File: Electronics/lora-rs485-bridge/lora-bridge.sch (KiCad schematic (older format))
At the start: 21 parts

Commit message: Some PCB routing is done
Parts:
- removed C?: C, symbol Device:C
- removed D4: NUP4004M5T1G, Housings_SOT-23_SOT-143_TSOT-6:SOT-23-5, symbol miceuz:TVS-ARRAY
- removed J?: USB_B_Micro, symbol Connector:USB_B_Micro
- added C10: 4.7u, Capacitor_SMD:C_0603_1608Metric, symbol Device:C
- added D1, D4: D_TVS_x2_AAC, miceuz-lib:SC89, symbol Device:D_TVS_x2_AAC
- added J9: USB micro, Connectors_USB:USB_Micro-B_Vertical_Molex-105133-0001, symbol Connector:USB_B_Micro
- C1, C2: renamed from C?; value C -> 22p; footprint (none) -> Capacitor_SMD:C_0603_1608Metric
- C3, C4, C5, C6, C8, C9: renamed from C?; value C -> 1u; footprint (none) -> Capacitor_SMD:C_0603_1608Metric
- J1: renamed from J?; footprint (none) -> TerminalBlock_RND:TerminalBlock_RND_205-00001_Pitch5.00mm
- J2: renamed from J?; footprint (none) -> Connector_Coaxial:SMA_Amphenol_901-144_Vertical; Manufacturer (none) -> TE Connectivity AMP Connectors; PartNo (none) -> 5-1814832-1
- J3, J4: renamed from J?; footprint (none) -> TerminalBlock_RND:TerminalBlock_RND_205-00003_Pitch5.00mm
- R1: renamed from R?; value R -> 10k; footprint (none) -> Resistor_SMD:R_0603_1608Metric
- SW1, SW2: renamed from SW?; footprint (none) -> Button_Switch_SMD:SW_Push_1P1T_NO_6x6mm_H9.5mm
- U2: renamed from U?; Manufacturer (none) -> Microchip; PartNo (none) -> ATSAMD21G18A-AUT
- U3: renamed from U?; Manufacturer (none) -> HopeRF; PartNo (none) -> RFM95W-868S2
- Y1: renamed from Y?; footprint (none) -> Crystals:Crystal_SMD_3215-2pin_3.2x1.5mm; Manufacturer (none) -> EPSON; PartNo (none) -> FC-135 32.7680KA-A5
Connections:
- net labels added: ANTENNA, DIO01, DIO02
- wire segments 55 -> 58

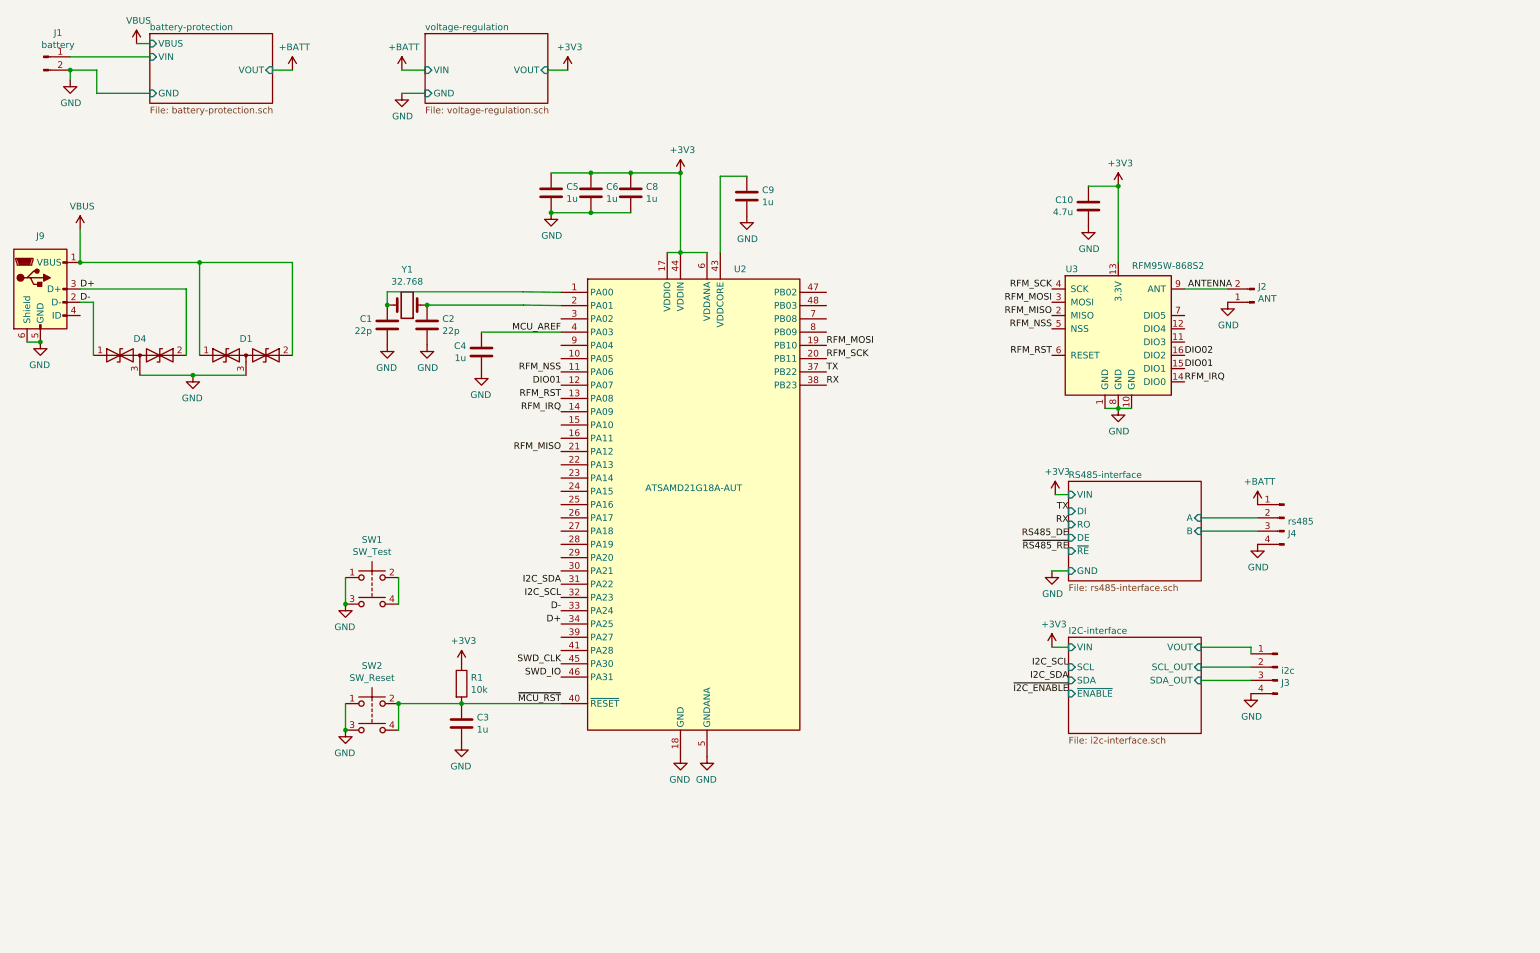
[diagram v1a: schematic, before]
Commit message: Add ESD protection to i2c lines, change VIN TVS diode to higher voltage, add series resistors to SPI lines, compress the PCB to be at width of typical 4xAA battery holder
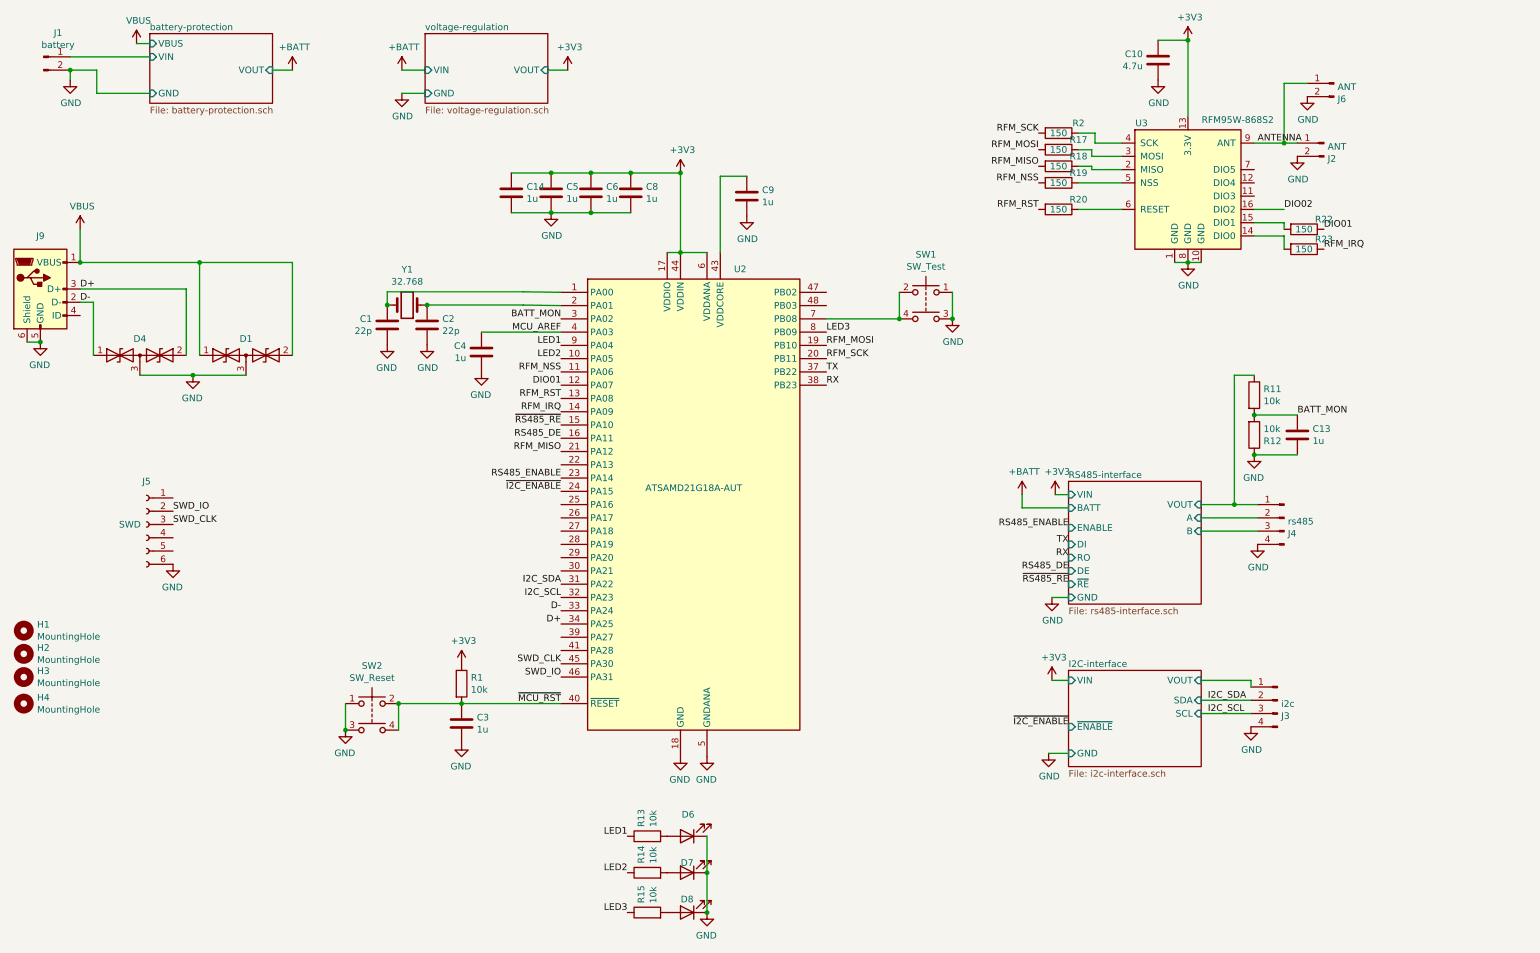
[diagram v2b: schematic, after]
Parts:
- added C13, C14: 1u, Capacitor_SMD:C_0603_1608Metric, symbol Device:C
- added D6, D7, D8: LED, LED_SMD:LED_0603_1608Metric, symbol Device:LED
- added H1, H2, H3, H4: MountingHole, Mounting_Holes:MountingHole_3.2mm_M3_DIN965, symbol Mechanical:MountingHole
- added J5: SWD, miceuz-lib:TC2030-MCP-NL, symbol Connector:Conn_01x06_Female
- added J6: ANT, miceuz-lib:U.FL_TEConnectivity_2334884_1, symbol Connector:Conn_01x02_Male
- added R11, R12, R13, R14, R15: 10k, Resistor_SMD:R_0603_1608Metric, symbol Device:R
- added R17, R18, R19, R2, R20, R22, R23: 150, Resistor_SMD:R_0603_1608Metric, symbol Device:R
- C10: Manufacturer SAMSUNG -> TDK; PartNo CL10A475KP8NNNC -> C1608X5R1C475K080AE
- J1: footprint TerminalBlock_RND:TerminalBlock_RND_205-00001_Pitch5.00mm -> TerminalBlock_MetzConnect:TerminalBlock_MetzConnect_Type101_RT01602HBWC_Pitch5.08mm
- J3, J4: footprint TerminalBlock_RND:TerminalBlock_RND_205-00003_Pitch5.00mm -> TerminalBlock_MetzConnect:TerminalBlock_MetzConnect_Type101_RT01604HBWC_Pitch5.08mm
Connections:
- net I2C-interface/SCL_OUT is gone; now on net I2C_SDA: J3.2 (Pin_2)
- net I2C-interface/SDA_OUT is gone; now on net I2C_SCL: J3.3 (Pin_3)
- net +3V3: now also C14.1
- net +BATT: no longer J4.1 (Pin_1)
- net ANTENNA: now also J2.1 (Pin_1), J6.1 (Pin_1); no longer J2.2 (Pin_2)
- net DIO01: now also R22.1; no longer U3.15 (DIO1)
- net GND: now also J2.2 (Pin_2), C13.2, C14.2, D6.1 (K), D7.1 (K), D8.1 (K), J5.6 (Pin_6), J6.2 (Pin_2), R12.1; no longer J2.1 (Pin_1)
- net RFM_IRQ: now also R23.1; no longer U3.14 (DIO0)
- net RFM_MISO: now also R18.2; no longer U3.2 (MISO)
- net RFM_MOSI: now also R17.2; no longer U3.3 (MOSI)
- net RFM_NSS: now also R19.2; no longer U3.5 (NSS)
- net RFM_RST: now also R20.2; no longer U3.6 (RESET)
- net RFM_SCK: now also R2.2; no longer U3.4 (SCK)
- net RS485_DE: now also U2.16 (PA11)
- net SWD_CLK: now also J5.3 (Pin_3)
- net SWD_IO: now also J5.2 (Pin_2)
- net ~I2C_ENABLE: now also U2.24 (PA15)
- net ~RS485_RE: now also U2.15 (PA10)
- net LED2: now reaches U2.10 (PA05)
- net LED2: now also R14.1
- net RS485_ENABLE: now reaches U2.23 (PA14)
- net BATT_MON: now reaches U2.3 (PA02)
- net BATT_MON: now also C13.1, R11.2, R12.2
- net at U2.7 (PB08): now also SW1.2, SW1.4
- net LED3: now reaches U2.8 (PB09)
- net LED3: now also R15.1
- net LED1: now reaches U2.9 (PA04)
- net LED1: now also R13.1
- new net: R23.2, U3.14 (DIO0)
- new net: R22.2, U3.15 (DIO1)
- new net: R18.1, U3.2 (MISO)
- new net: R17.1, U3.3 (MOSI)
- new net: R2.1, U3.4 (SCK)
- new net: R19.1, U3.5 (NSS)
- new net: R20.1, U3.6 (RESET)
- new net: D6.2 (A), R13.2
- new net: D8.2 (A), R15.2
- new net: D7.2 (A), R14.2
- new net RS485-interface/VOUT: J4.1 (Pin_1), R11.1
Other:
- moved on the sheet: C10, J2, J3, SW1, U3

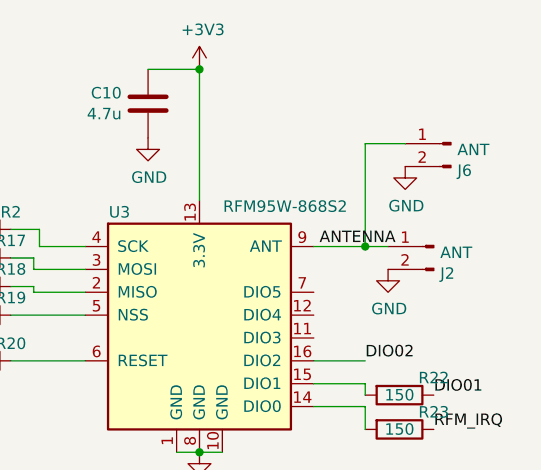
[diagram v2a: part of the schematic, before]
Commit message: Add power input PTC fuse
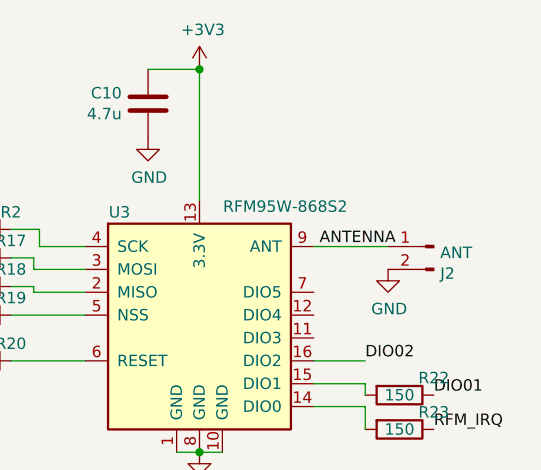
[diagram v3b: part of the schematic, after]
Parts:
- removed J6: ANT, miceuz-lib:U.FL_TEConnectivity_2334884_1, symbol Connector:Conn_01x02_Male
- J2: footprint Connector_Coaxial:SMA_Amphenol_901-144_Vertical -> Connector_Coaxial:SMA_Amphenol_132289_EdgeMount
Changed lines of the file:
@@
 encoding utf-8
 Sheet 1 5
-Title ""
-Date ""
-Rev ""
-Comp ""
-Comment1 ""
+Title "Lora - RS485 bridge"
+Date "2019-11-05"
+Rev "1.1"
+Comp "Albertas Mickenas"
+Comment1 "albertas@technarium.lt"
 Comment2 ""
 Comment3 ""
@@
 F 0 "J2" H 10597 1582 50  0000 R CNN
 F 1 "ANT" H 10597 1673 50  0000 R CNN
-F 2 "Connector_Coaxial:SMA_Amphenol_901-144_Vertical" H 10625 1700 50  0001 C CNN
+F 2 "Connector_Coaxial:SMA_Amphenol_132289_EdgeMount" H 10625 1700 50  0001 C CNN
 F 3 "~" H 10625 1700 50  0001 C CNN
 F 4 "5-1814832-1" H 10625 1700 50  0001 C CNN "PartNo"
@@
 	-1   0    0    -1
 $EndComp
-Wire Wire Line
-	10100 1700 10325 1700
 $Comp
 L power:GND #PWR0116
@@
 Connection ~ 7425 3025
 $Comp
-L power:GND #PWR0136
-U 1 1 5D8D97A9
-P 10500 1350
-F 0 "#PWR0136" H 10500 1100 50  0001 C CNN
-F 1 "GND" H 10505 1177 50  0000 C CNN
-F 2 "" H 10500 1350 50  0001 C CNN
-F 3 "" H 10500 1350 50  0001 C CNN
-	1    10500 1350
-	1    0    0    -1
-$EndComp
-$Comp
-L Connector:Conn_01x02_Male J6
-U 1 1 5D8D9796
-P 10700 1250
-F 0 "J6" H 10672 1132 50  0000 R CNN
-F 1 "ANT" H 10672 1223 50  0000 R CNN
-F 2 "miceuz-lib:U.FL_TEConnectivity_2334884_1" H 10700 1250 50  0001 C CNN
-F 3 "~" H 10700 1250 50  0001 C CNN
-F 4 "2334884-1" H 10700 1250 50  0001 C CNN "PartNo"
-F 5 "TE Connectivity AMP Connectors" H 10700 1250 50  0001 C CNN "Manufacturer"
-	1    10700 1250
-	-1   0    0    -1
-$EndComp
-Wire Wire Line
-	10500 1250 10325 1250
-Wire Wire Line
-	10325 1250 10325 1700
-Connection ~ 10325 1700
-Wire Wire Line
-	10325 1700 10425 1700
-$Comp
 L power:GND #PWR01
 U 1 1 5DAFB4A2
@@
 Wire Wire Line
 	10325 2400 10325 2500
+Wire Wire Line
+	10100 1700 10425 1700
 $EndSCHEMATC

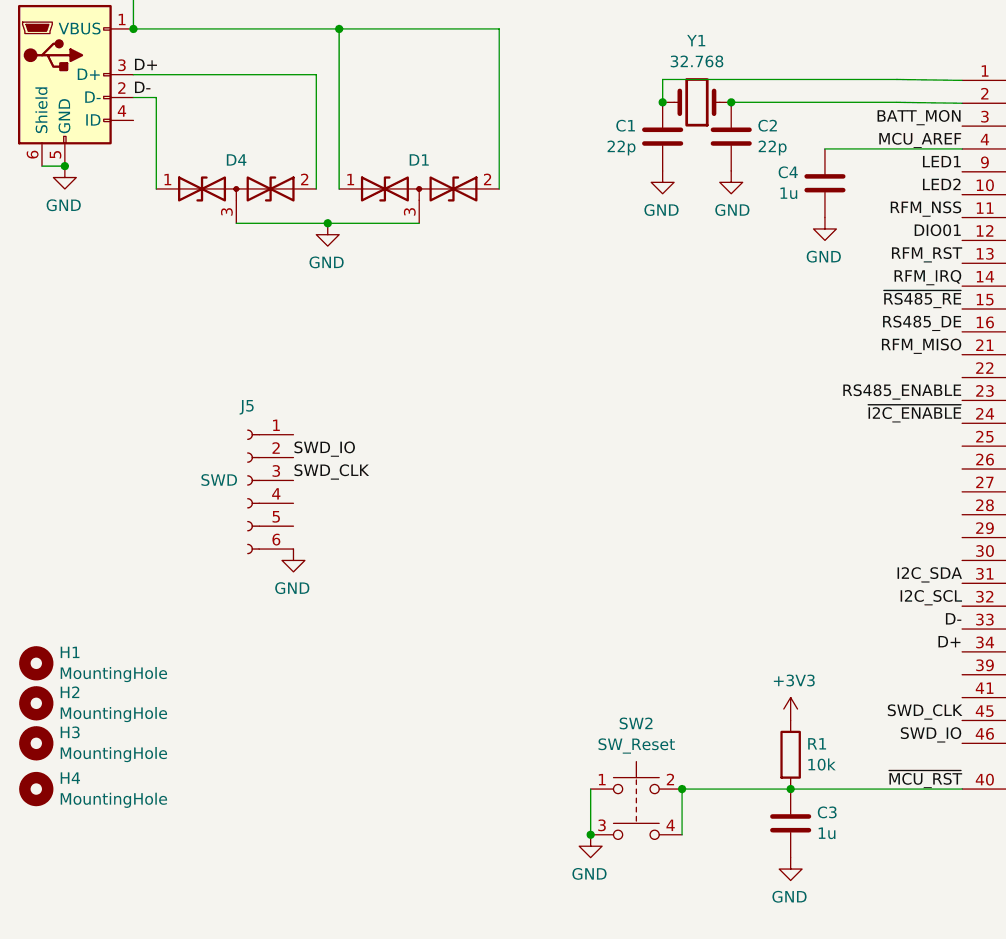
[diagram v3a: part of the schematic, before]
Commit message: Add pullup to SWDCLK for better stability. Change reset pullup value to 1k
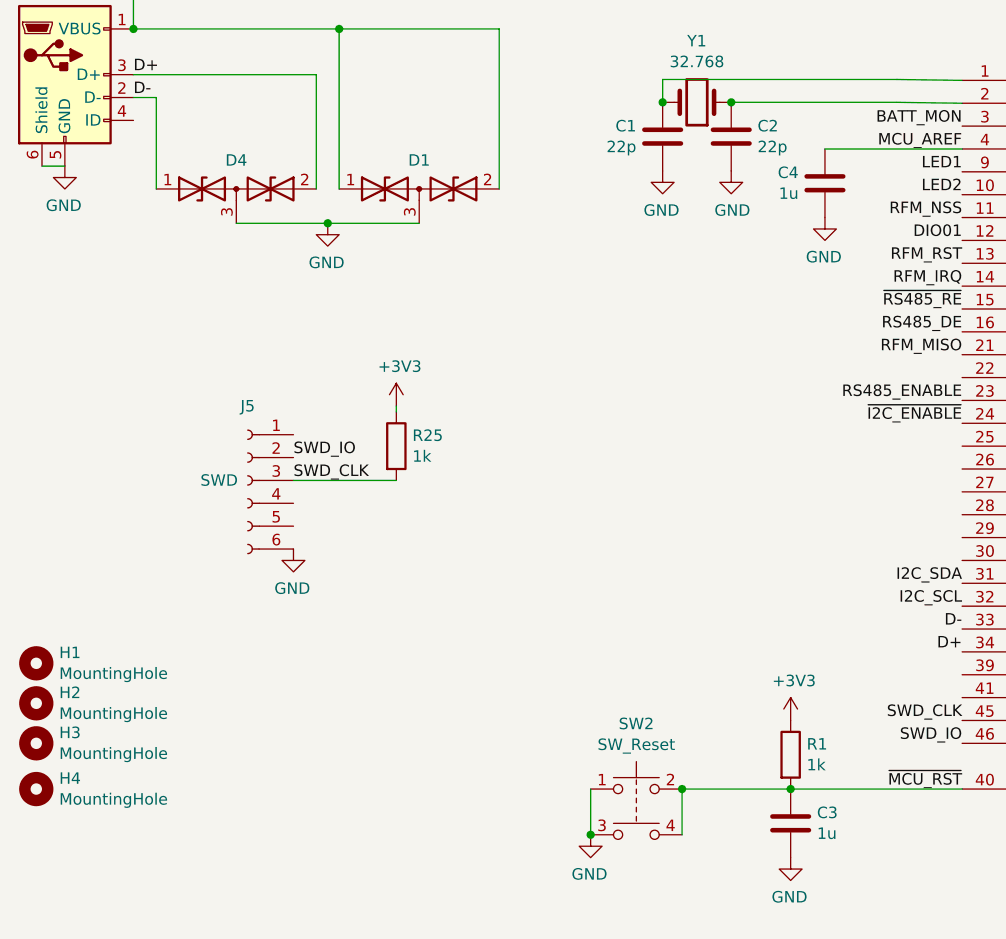
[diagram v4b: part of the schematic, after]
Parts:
- added R25: 1k, Resistor_SMD:R_0603_1608Metric, symbol Device:R
- R1: value 10k -> 1k
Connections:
- net +3V3: now also R25.1
- net SWD_CLK: now also R25.2
